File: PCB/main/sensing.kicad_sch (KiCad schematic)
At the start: 0 parts

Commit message: 4TH WEEK, CHANGES FOR SENSING
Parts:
- added C1, C2: 1uF, symbol Device:C_Small
- added R1, R2, R3, R4, R5, R6: 1k, symbol Device:R_Small_US
- added U1, U2: LTR-303ALS-01, OptoDevice:Lite-On_LTR-303ALS-01, symbol Sensor_Optical:LTR-303ALS-01
- added U3: 4011, symbol 4xxx:4011
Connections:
- new net: U3.1, U3.5
- new net: U3.2, U3.6
- new net GND: C1.2, C2.2, U1.3 (GND), U2.3 (GND)
- new net Vbus: R1.1, R2.1, R3.1, R4.1, R5.1, R6.1
- new net power supply: C1.1, C2.1, U1.1 (VDD), U2.1 (VDD)
- new net uController INT PB12: U3.3, U3.4
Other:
- note added: "2022/03/12"
- note added: "Light Sensor"
- note added: "Masonwabe Nkombisa"

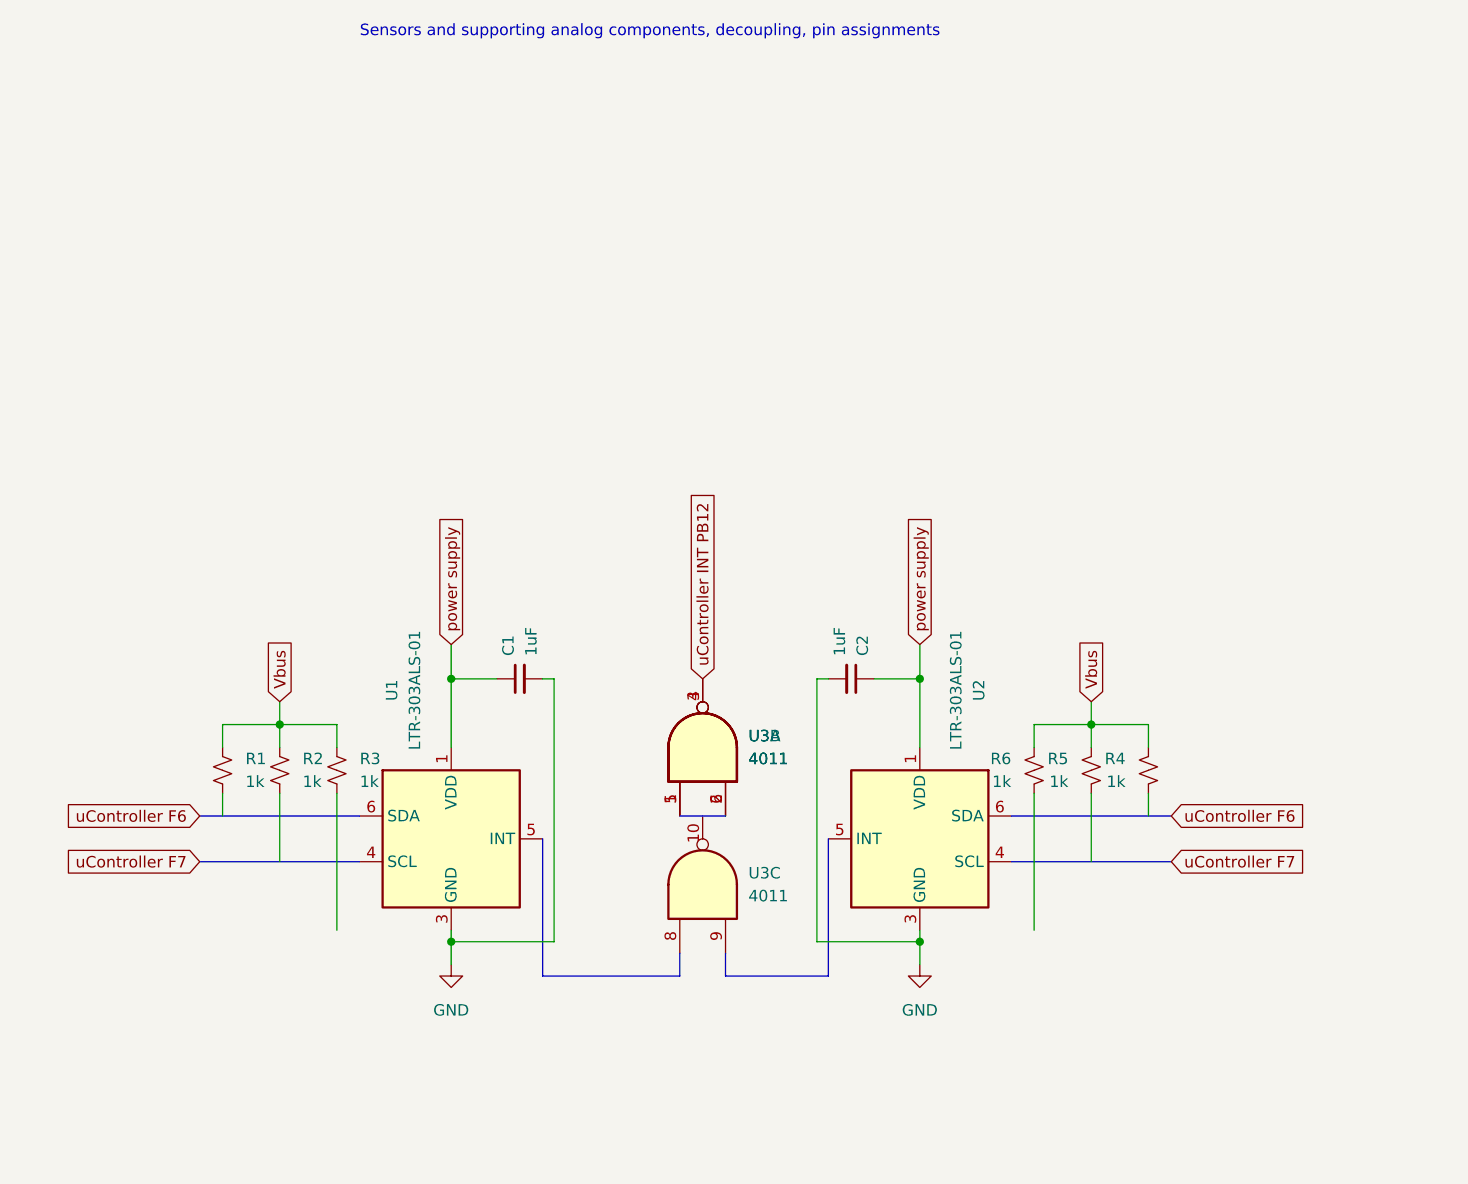
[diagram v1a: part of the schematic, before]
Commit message: Week 5 submission, with improved version of the sensor
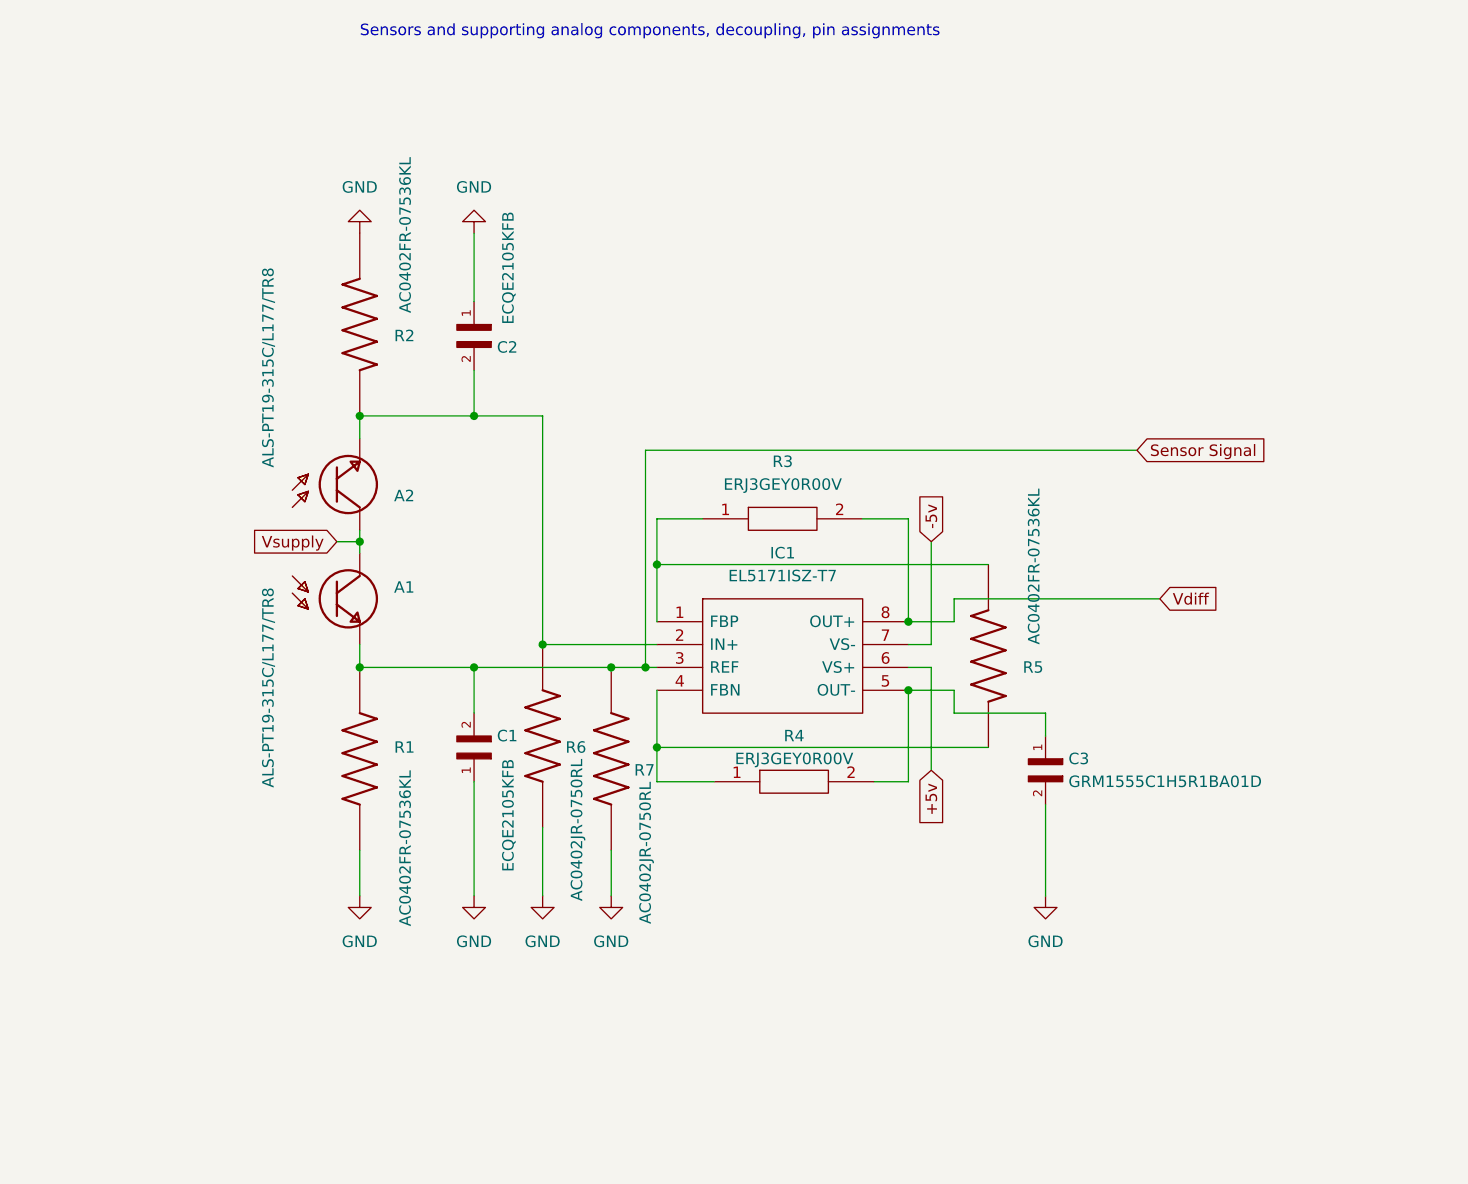
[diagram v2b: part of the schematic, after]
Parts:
- removed C1, C2: 1uF, symbol Device:C_Small
- removed R1, R2, R3, R4, R5, R6: 1k, symbol Device:R_Small_US
- removed U1, U2: LTR-303ALS-01, OptoDevice:Lite-On_LTR-303ALS-01, symbol Sensor_Optical:LTR-303ALS-01
- removed U3: 4011, symbol 4xxx:4011
- added A1, A2: ALS-PT19-315C/L177/TR8, XDCR_ALS-PT19-315C/L177/TR8, symbol ALS-PT19-315C_L177_TR8:ALS-PT19-315C/L177/TR8
- added C1, C2: ECQE2105KFB, CAPRR1000W80L1850T740H2000, symbol ECQE2105KFB:ECQE2105KFB
- added C3: GRM1555C1H5R1BA01D, CAPC1005X55N, symbol GRM1555C1H5R1BA01D:GRM1555C1H5R1BA01D
- added IC1: EL5171ISZ-T7, SOIC127P600X175-8N, symbol SamacSys_Parts:EL5171ISZ-T7
- added R1, R2, R5: AC0402FR-07536KL, RESC1005X37N, symbol AC0402FR-07536KL:AC0402FR-07536KL
- added R3, R4: ERJ3GEY0R00V, ERJ3EKF1000V, symbol SamacSys_Parts:ERJ3GEY0R00V
- added R6, R7: AC0402JR-0750RL, RESC1005X37N, symbol AC0402JR-0750RL:AC0402JR-0750RL
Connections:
- net GND: now also C1.1, C2.1, C3.2, R1.1, R2.1, R6.1, R7.1
- new net: C3.1, IC1.5 (OUT-), R4.2
- new net: IC1.4 (FBN), R4.1, R5.2
- new net: A2.2, C2.2, IC1.2 (IN+), R2.2, R6.2
- new net: IC1.1 (FBP), R3.1, R5.1
- new net +5v: IC1.6 (VS+)
- new net -5v: IC1.7 (VS-)
- new net Sensor Signal: A1.2, C1.2, IC1.3 (REF), R1.2, R7.2
- new net Vdiff: IC1.8 (OUT+), R3.2
- new net Vsupply: A1.1, A2.1

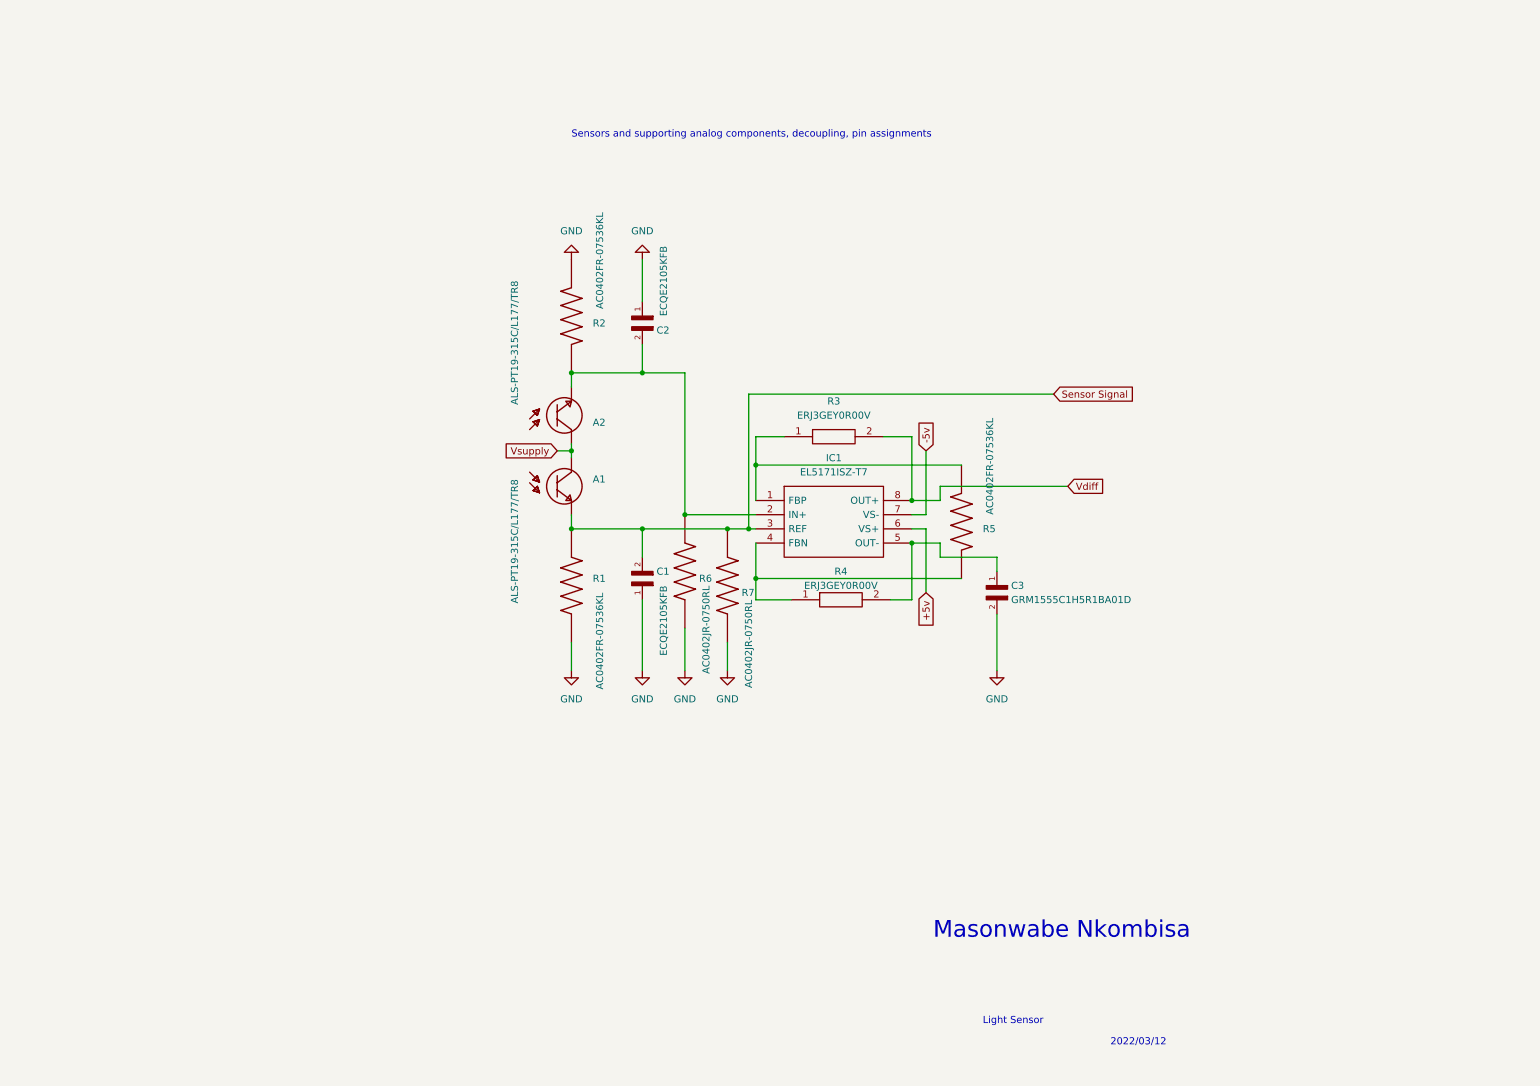
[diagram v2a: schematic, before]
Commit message: Sensing module combined with main module
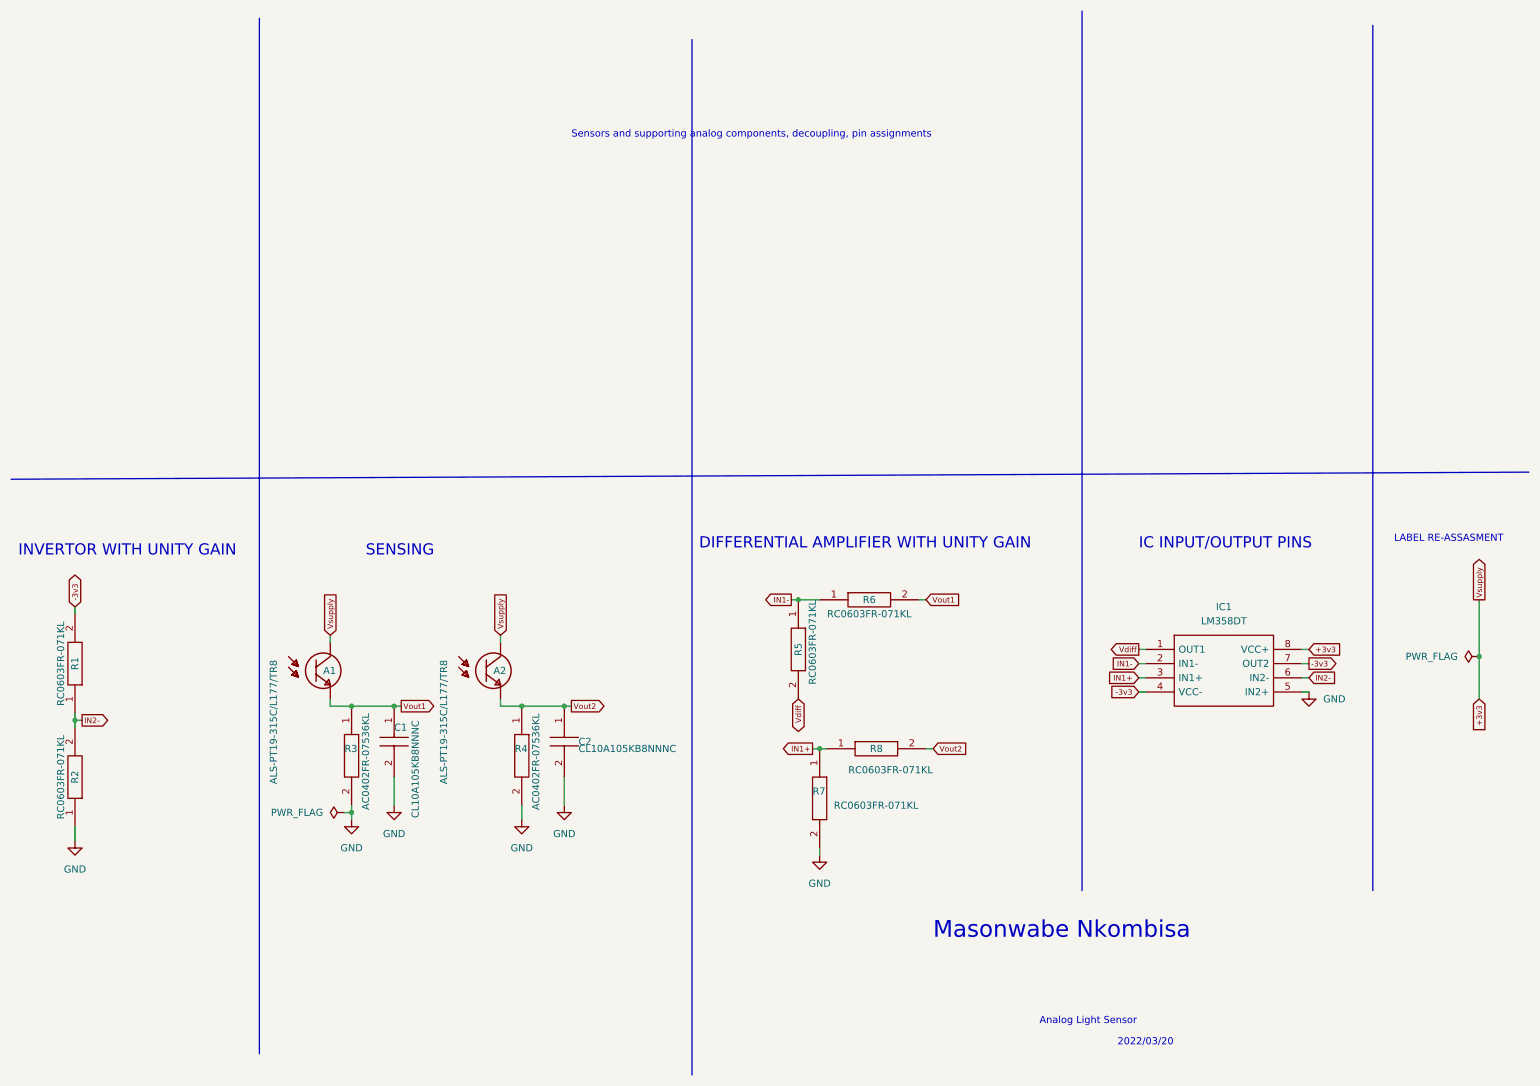
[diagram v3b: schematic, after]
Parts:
- removed C1, C2: ECQE2105KFB, CAPRR1000W80L1850T740H2000, symbol ECQE2105KFB:ECQE2105KFB
- removed C3: GRM1555C1H5R1BA01D, CAPC1005X55N, symbol GRM1555C1H5R1BA01D:GRM1555C1H5R1BA01D
- removed IC1: EL5171ISZ-T7, SOIC127P600X175-8N, symbol SamacSys_Parts:EL5171ISZ-T7
- removed R1, R2, R5: AC0402FR-07536KL, RESC1005X37N, symbol AC0402FR-07536KL:AC0402FR-07536KL
- removed R3, R4: ERJ3GEY0R00V, ERJ3EKF1000V, symbol SamacSys_Parts:ERJ3GEY0R00V
- removed R6, R7: AC0402JR-0750RL, RESC1005X37N, symbol AC0402JR-0750RL:AC0402JR-0750RL
- added C1, C2: CL10A105KB8NNNC, SamacSys_Parts:CAPC1608X90N, symbol SamacSys_Parts:CL10A105KB8NNNC
- added IC1: LM358DT, SamacSys_Parts:SOIC127P600X175-8N, symbol SamacSys_Parts:LM358DT
- added R1, R2, R5, R6, R7, R8: RC0603FR-071KL, SamacSys_Parts:RESC1608X55N, symbol SamacSys_Parts:RC0603FR-071KL
- added R3, R4: AC0402FR-07536KL, SamacSys_Parts:RESC1005X37N, symbol SamacSys_Parts:AC0402FR-07536KL
- A1, A2: footprint XDCR_ALS-PT19-315C/L177/TR8 -> SamacSys_Parts:XDCR_ALS-PT19-315C_L177_TR8
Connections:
- net GND: now also C1.2, C2.2, IC1.5 (IN2+), R2.1, R3.2, R4.2, R7.2
- net Vdiff: now also IC1.1 (OUT1), R5.2
- net Vout2: now reaches A2.2
- net Vout2: now also C2.1, R4.1, R8.2
- net Sensor Signal renamed Vout1
- net Vout1: now also C1.1, R3.1, R6.2
- net Vsupply renamed +3v3
- net +3v3: now also IC1.8 (VCC+)
- new net -3v3: IC1.4 (VCC-), IC1.7 (OUT2), R1.2
- new net IN1+: IC1.3 (IN1+), R7.1, R8.1
- new net IN1-: IC1.2 (IN1-), R5.1, R6.1
- new net IN2-: IC1.6 (IN2-), R1.1, R2.2
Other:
- note added: "2022/03/20"
- note added: "Analog Light Sensor"
- note added: "DIFFERENTIAL AMPLIFIER WITH UNITY GAIN"
- note added: "IC INPUT/OUTPUT PINS"
- note added: "INVERTOR WITH UNITY GAIN"
- note added: "LABEL RE-ASSASMENT"
- note added: "SENSING"
- note removed: "2022/03/12"
- note removed: "Light Sensor"
